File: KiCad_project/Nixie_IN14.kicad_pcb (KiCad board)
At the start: 2 copper layers, 148.3 x 69.3 mm, 65 parts, among them J1 Conn_01x10_Pin, J2 Conn_01x07_Pin, J3 Conn_01x07_Pin, J4 Conn_01x10_Pin, J5 Conn_01x07_Pin, J6 Conn_01x07_Pin, J7 USB_C_Receptacle_PowerOnly_6P, Q1 IRF540N, Q2 MMBTA42, U1 BME280_module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

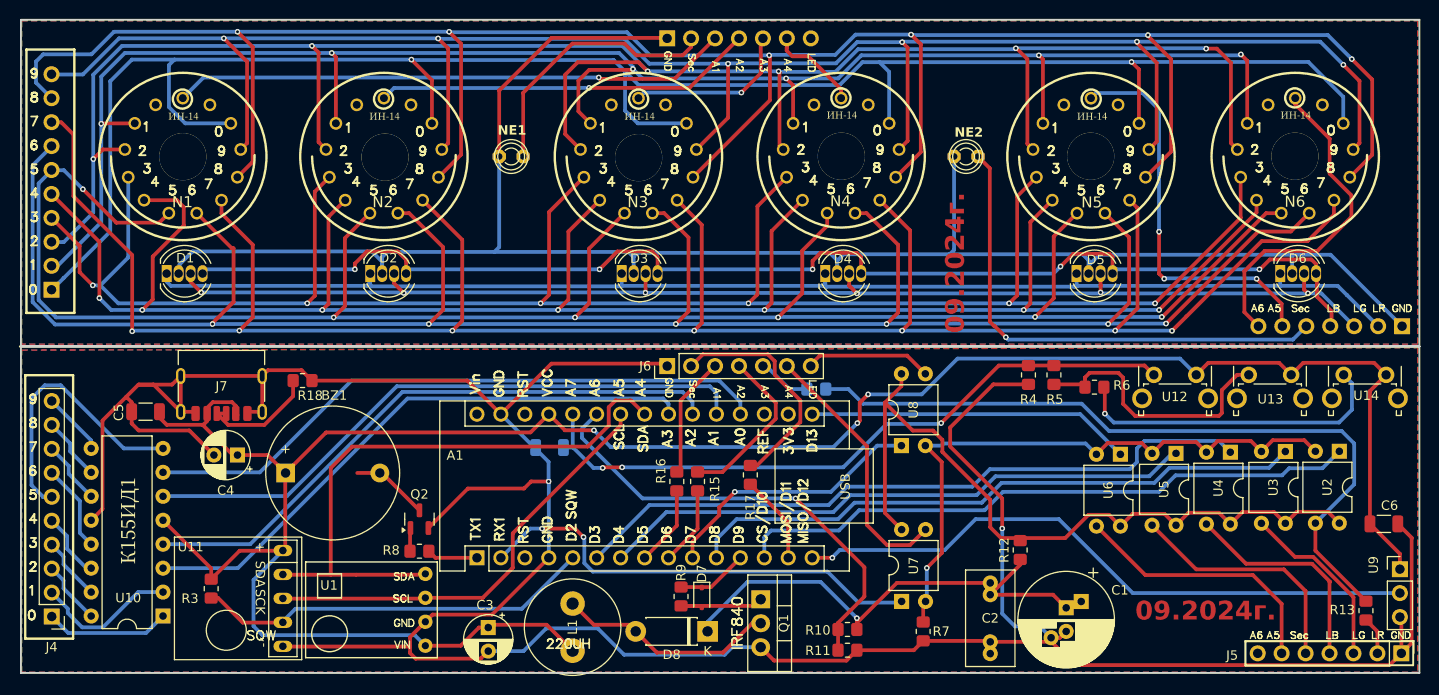
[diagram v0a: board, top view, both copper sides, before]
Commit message: fixed connection error replaced and rerouted
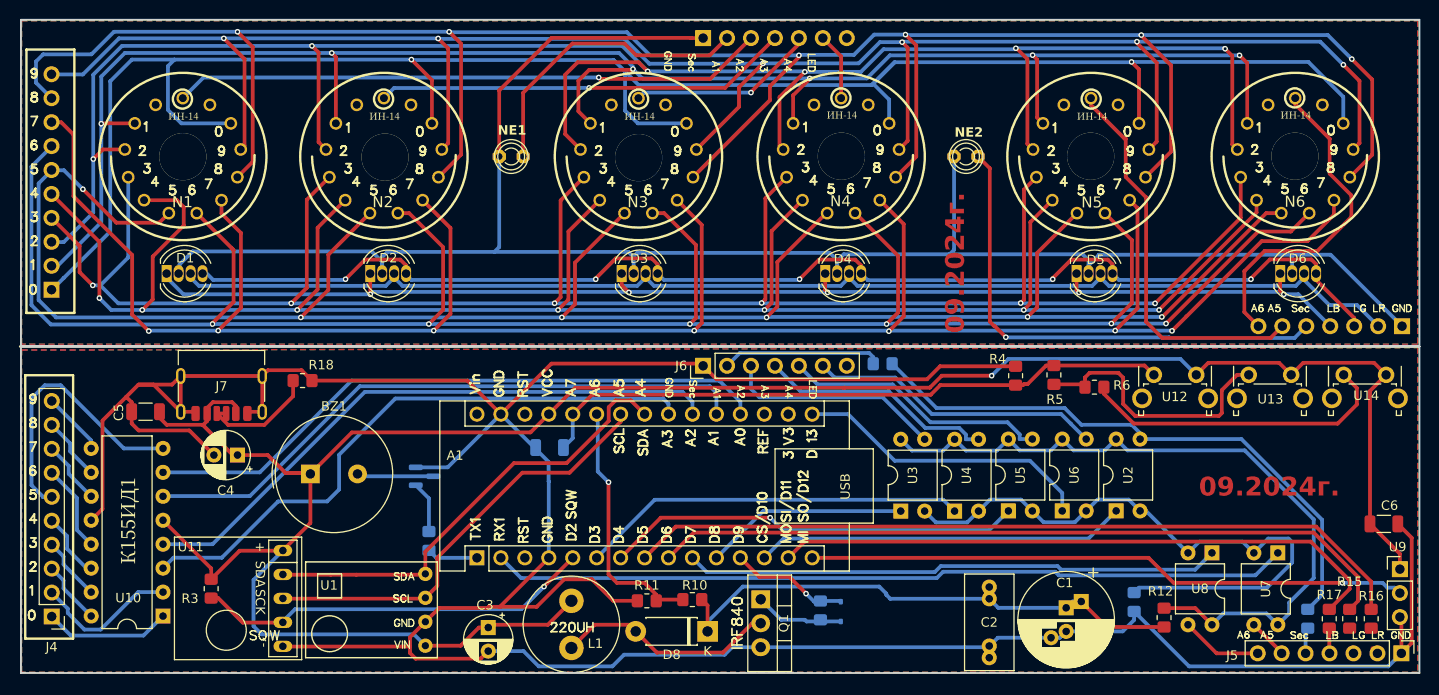
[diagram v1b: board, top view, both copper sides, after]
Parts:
- BZ1: footprint Buzzer_Beeper:Buzzer_D14mm_H7mm_P10mm -> Buzzer_Beeper:Buzzer_TDK_PS1240P02BT_D12.2mm_H6.5mm
- D7, Q2, R13, R7, R8, R9: moved to B.Cu
- moved R16 75.1 mm to (209.3, 118.7), turned to -90 degrees
- moved R15 70.7 mm to (207.0, 118.7), turned to -90 degrees
- moved R17 63.3 mm to (204.9, 118.7), turned to -90 degrees
- moved R13 57.6 mm to (157.5, 91.7), turned to 180 degrees
- moved R14 57.5 mm to (202.6, 118.7), turned to -90 degrees
- moved U3 41.3 mm to (159.4, 107.3), turned to 90 degrees
- moved U7 40.2 mm to (199.4, 111.8), turned to -90 degrees
- moved U8 34.8 mm to (192.4, 111.8), turned to -90 degrees
- moved U4 29.9 mm to (165.1, 107.3), turned to 90 degrees
- moved U2 24.5 mm to (182.2, 107.3), turned to 90 degrees
- moved R7 22.6 mm to (184.2, 117.0)
- moved R11 21.9 mm to (132.5, 116.8), turned to 0 degrees
- moved U5 18.8 mm to (170.8, 107.3), turned to 90 degrees
- moved R12 16.9 mm to (187.3, 118.6)
- moved R10 16.8 mm to (137.3, 116.7)
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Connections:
- J3 pad 2: LED_R_top -> LED_G_top
- J3 pad 3: LED_G_top -> LED_B_top
- J3 pad 4: LED_B_top -> LED_R_top
- J5 pad 2: SEC_1 -> LED_G
- J5 pad 3: A1 -> LED_B
- J5 pad 4: A2 -> LED_R
- J5 pad 5: A3 -> SEC_2
- J5 pad 6: A4 -> A5
- J5 pad 7: LED_B_NCC -> A6
- J6 pad 2: LED_R -> SEC_1
- J6 pad 3: LED_G -> A1
- J6 pad 4: LED_B -> A2
- J6 pad 5: SEC_2 -> A3
- J6 pad 6: A5 -> A4
- J6 pad 7: A6 -> LED_B_NCC
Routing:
- net Net-(A1-D5): track 8.52 -> 83.8 mm
- net Net-(A1-D6): track 8.38 -> 80.0 mm
- net Net-(A1-D11): track 9.47 -> 65.9 mm
- net A1_CONTROL: track 66.2 -> 21.6 mm
- net A5_CONTROL: track 48.5 -> 84.7 mm, vias 2 -> 0
- net A2_CONTROL: track 73.7 -> 41.0 mm
- net A6_CONTROL: track 28.6 -> 56.9 mm, vias 1 -> 0
- net SEC_CONTROL: track 67.0 -> 39.4 mm
- net A5: track 28.2 -> 4.25 mm
- net CHECK_PWR: track 48.8 -> 27.0 mm
- net LED_R: track 24.5 -> 3.00 mm
- net A3_CONTROL: track 63.5 -> 44.3 mm, vias 0 -> 1
- net LED_B: track 17.8 -> 0.57 mm
- net Net-(R13-Pad1): track 79.1 -> 63.0 mm
- net SDA: track 64.5 -> 48.9 mm
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
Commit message: minor routing optimization
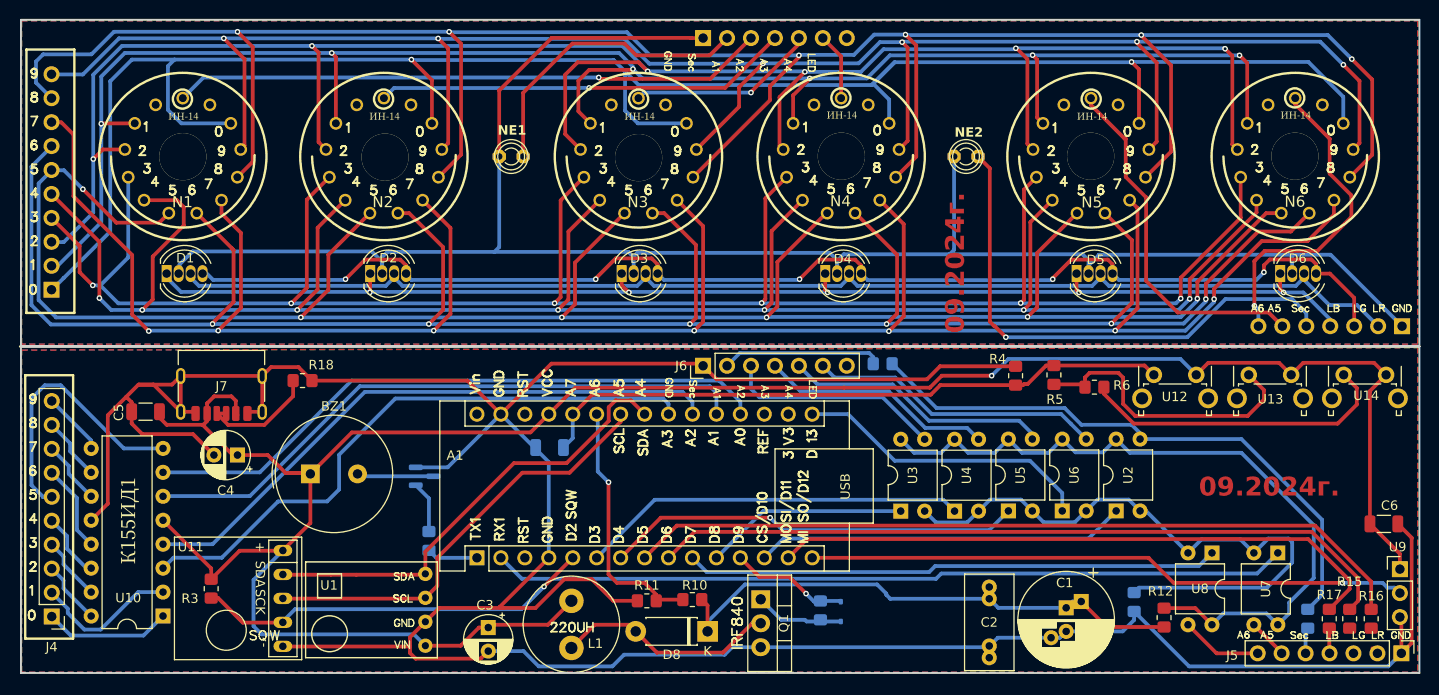
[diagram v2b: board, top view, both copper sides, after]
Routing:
- net A5_top: track 41.9 -> 38.3 mm
- net SEC_2_top: track 52.8 -> 56.0 mm
- net Net-(R5-Pad2): track 28.8 -> 31.2 mm
- net Net-(J1-Pin_4): track 210.5 -> 211.8 mm
- net LED_B_top: track 137.0 -> 138.2 mm
- net Net-(J1-Pin_5): track 212.6 -> 213.9 mm
- net Net-(J1-Pin_6): track 221.5 -> 222.7 mm
- net +5V: track 245.3 -> 246.4 mm
- net Net-(J1-Pin_7): track 231.0 -> 232.0 mm
- net Net-(J1-Pin_8): track 236.9 -> 237.9 mm
- net A6_top: track 35.3 -> 34.4 mm, vias 0 -> 1
- net GNDREF: track 355.2 -> 355.9 mm

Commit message: added power keys for LEDs resistor pacjakges changed from 0805 to 1206
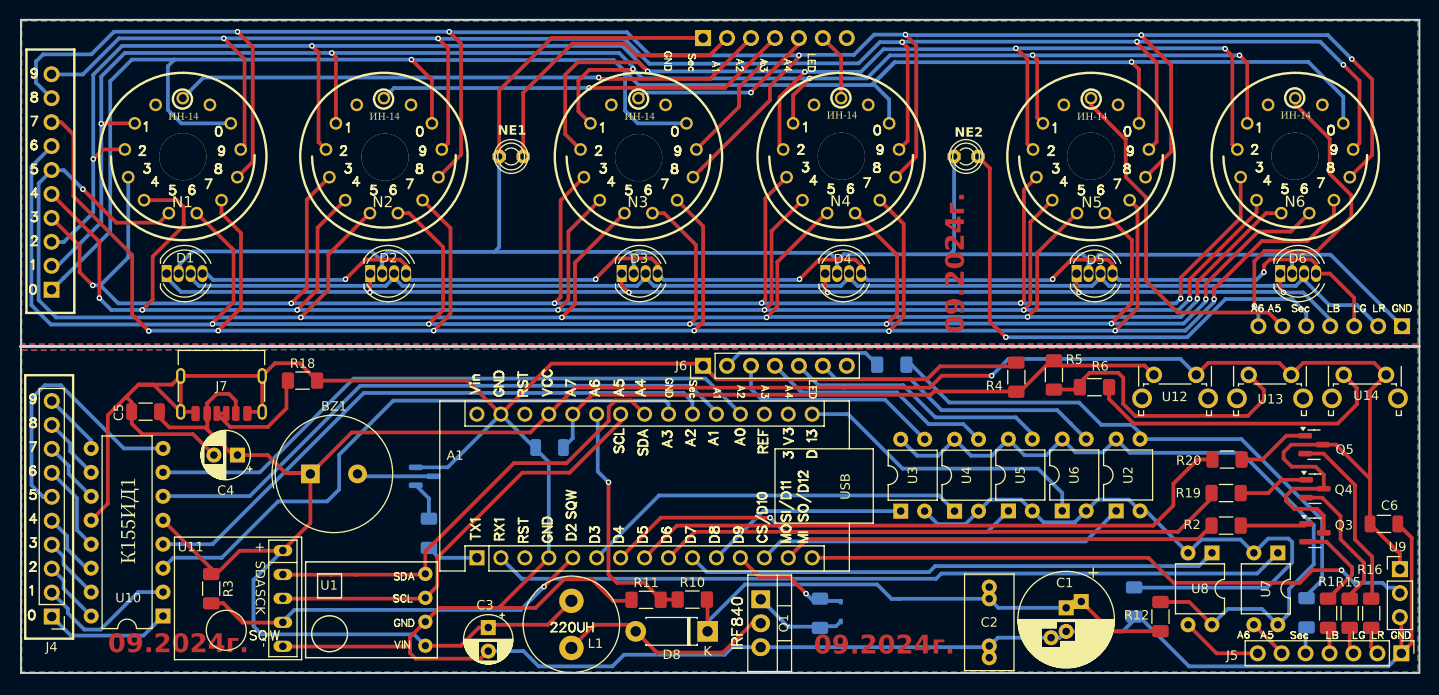
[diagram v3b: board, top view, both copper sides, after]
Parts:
- removed R17: 51, Resistor_SMD:R_0805_2012Metric_Pad1.20x1.40mm_HandSolder
- added Q3: MMBTA42, Package_TO_SOT_SMD:SOT-23, F.Cu at (203.3, 109.6)
- added Q4: MMBTA42, Package_TO_SOT_SMD:SOT-23, F.Cu at (203.3, 105.0)
- added Q5: MMBTA42, Package_TO_SOT_SMD:SOT-23, F.Cu at (203.2, 100.3)
- added R1: 51, Resistor_SMD:R_1206_3216Metric_Pad1.30x1.75mm_HandSolder, F.Cu at (204.7, 118.2)
- added R19: 2.2k, Resistor_SMD:R_1206_3216Metric_Pad1.30x1.75mm_HandSolder, F.Cu at (193.9, 105.4)
- added R2: 2.2k, Resistor_SMD:R_1206_3216Metric_Pad1.30x1.75mm_HandSolder, F.Cu at (193.9, 108.9)
- added R20: 2.2k, Resistor_SMD:R_1206_3216Metric_Pad1.30x1.75mm_HandSolder, F.Cu at (194.0, 101.9)
- R10, R11, R12, R13, R14, R15, R16, R18, R3, R4, R5, R6, R7, R8, R9: footprint Resistor_SMD:R_0805_2012Metric_Pad1.20x1.40mm_HandSolder -> Resistor_SMD:R_1206_3216Metric_Pad1.30x1.75mm_HandSolder
- moved R13 0.97 mm to (158.4, 91.8)
- moved R8 0.81 mm to (109.3, 109.7)
- moved R14 0.65 mm to (202.4, 118.1)
- moved R15 0.58 mm to (207.0, 118.2)
- moved R16 0.58 mm to (209.3, 118.2)
- moved R12 0.39 mm to (186.9, 118.5)
- moved R9 0.31 mm to (150.8, 118.2)
- moved R4 0.17 mm to (171.7, 93.1)
- moved R11 0.13 mm to (132.4, 116.7)
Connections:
- A1 pad 14: Net-(A1-D11) -> LED_R_CONTROL
- A1 pad 8: Net-(A1-D5) -> LED_G_CONTROL
- A1 pad 9: Net-(A1-D6) -> LED_B_CONTROL
- R15 pad 1: Net-(A1-D6) -> Net-(Q4-E)
- R16 pad 1: Net-(A1-D5) -> Net-(Q5-E)
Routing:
- net Net-(A1-D5): track 83.9 -> 0.00 mm
- net Net-(A1-D6): track 80.0 -> 0.00 mm
- net Net-(A1-D11): track 66.2 -> 0.00 mm
- net LED_G_CONTROL: track 0.00 -> 65.9 mm
- net LED_B_CONTROL: track 0.00 -> 60.8 mm
- net LED_R_CONTROL: track 0.00 -> 46.3 mm
- net +5V: track 246.4 -> 275.6 mm
- net Net-(Q5-E): track 0.00 -> 19.5 mm
- net Net-(Q4-E): track 0.00 -> 14.9 mm
- net Net-(Q3-E): track 0.00 -> 10.4 mm
- net Net-(Q5-B): track 0.00 -> 7.78 mm
- net Net-(Q4-B): track 0.00 -> 7.52 mm
- net Net-(Q3-B): track 0.00 -> 7.02 mm
- net Net-(R13-Pad1): track 63.0 -> 60.3 mm
- net LED_B: track 0.57 -> 2.83 mm
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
